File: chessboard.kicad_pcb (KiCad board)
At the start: 4 copper layers, 34 parts, among them U2 XIAO-RP2040-DIP, U3 ST25R3911B-AQW, Y3 27.12 MHz

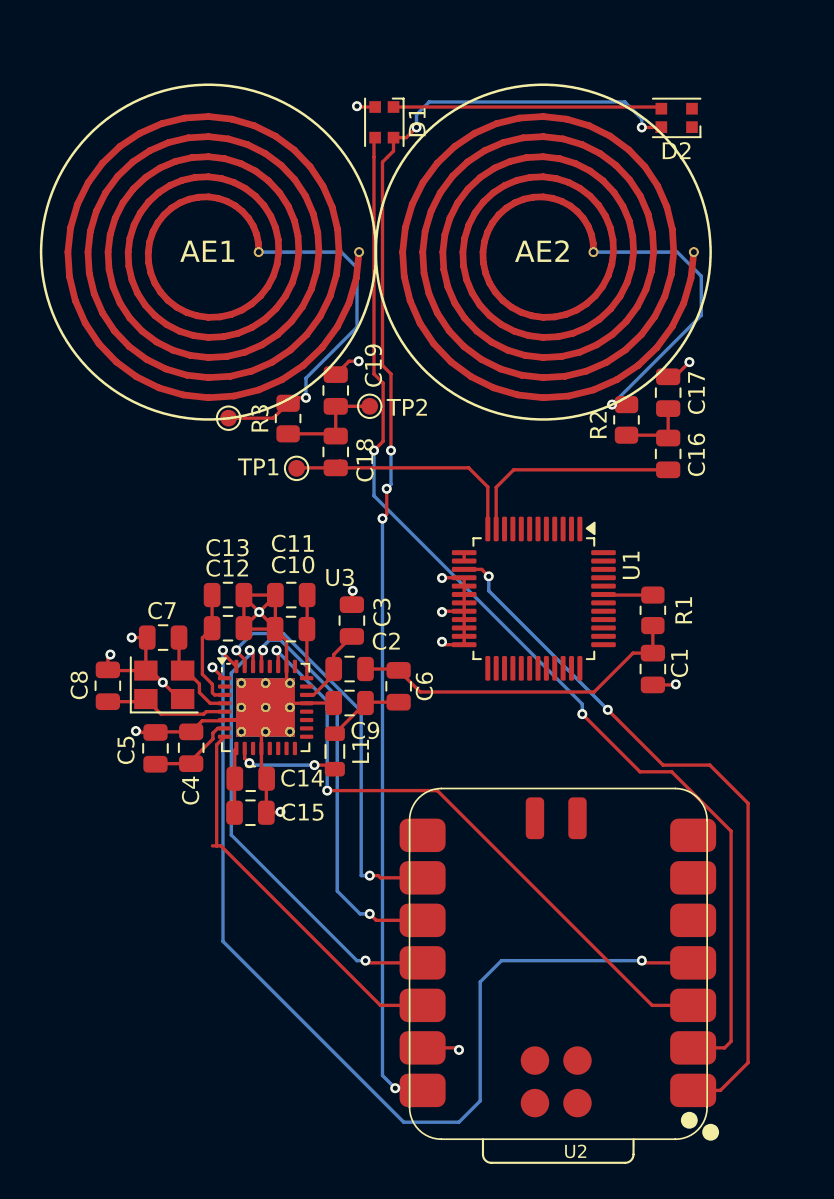
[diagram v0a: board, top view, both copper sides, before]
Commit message: Add QR code
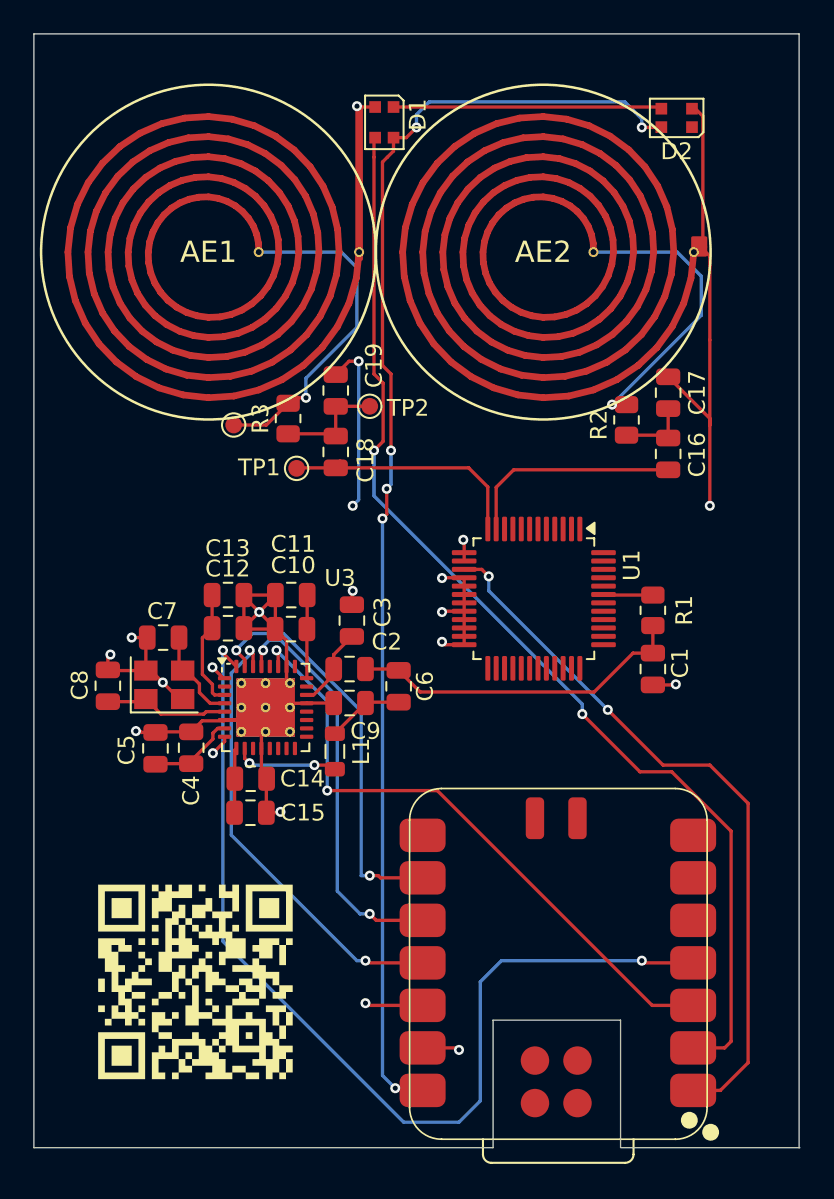
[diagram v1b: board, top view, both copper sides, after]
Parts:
- added G***: LOGO, LOGO, F.Cu at (109.2, 133.6)
- moved TP3 0.51 mm to (111.5, 100.3)
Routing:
- net GND: track 61.2 -> 97.1 mm, vias 15 -> 16
- net +3.3V: track 24.7 -> 7.07 mm, vias 1 -> 4
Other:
- board outline added: 45.8 x 66.5 mm
